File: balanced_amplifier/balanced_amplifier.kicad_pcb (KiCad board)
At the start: 2 copper layers, 100 x 100 mm, 117 parts, among them J1 Conn_01x04_Male, J2 Conn_01x04_Male, J3 Screw_Terminal_01x03, J4 Conn_01x04_Male, J5 Conn_01x04_Male, U1 LM4562, U2 LM4562, U3 NE5532, U4 LM4562, U5 LM4562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

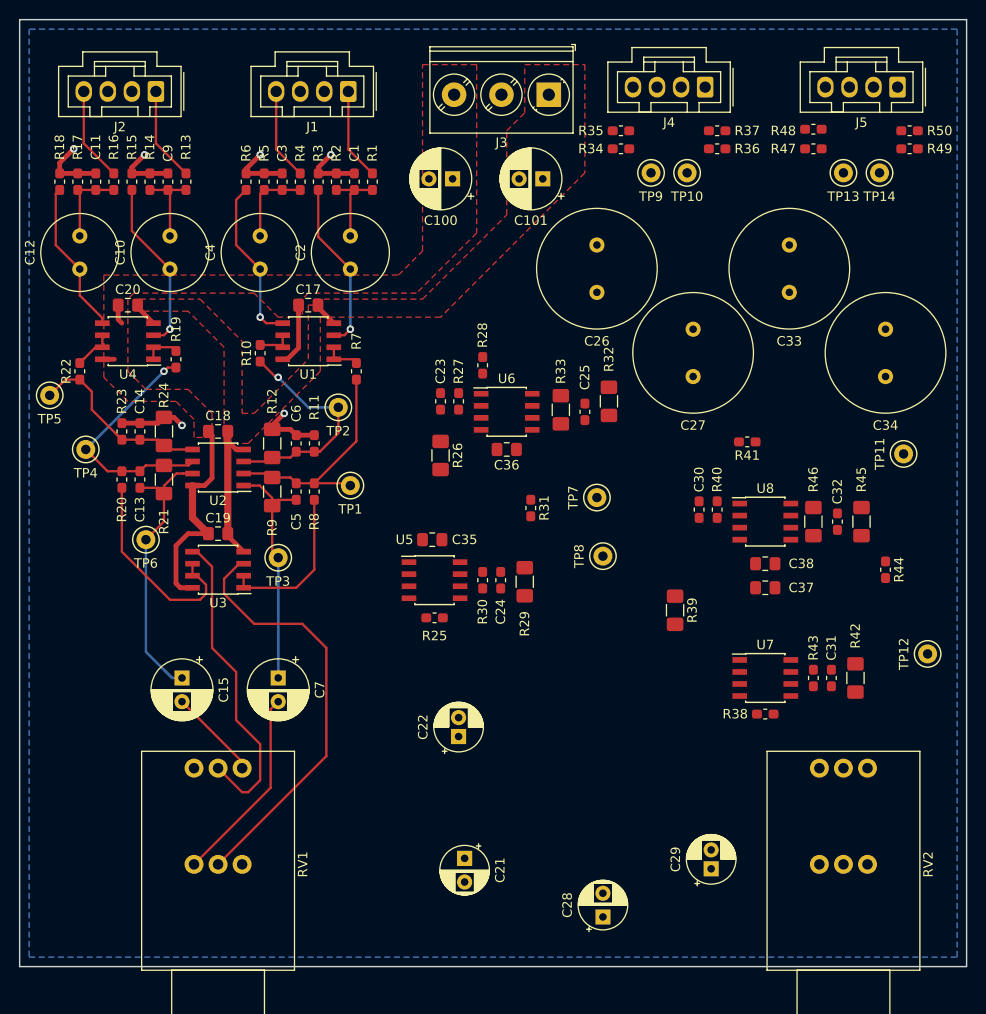
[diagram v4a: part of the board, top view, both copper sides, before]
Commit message: initial layout complete; all connections made & passes DRC
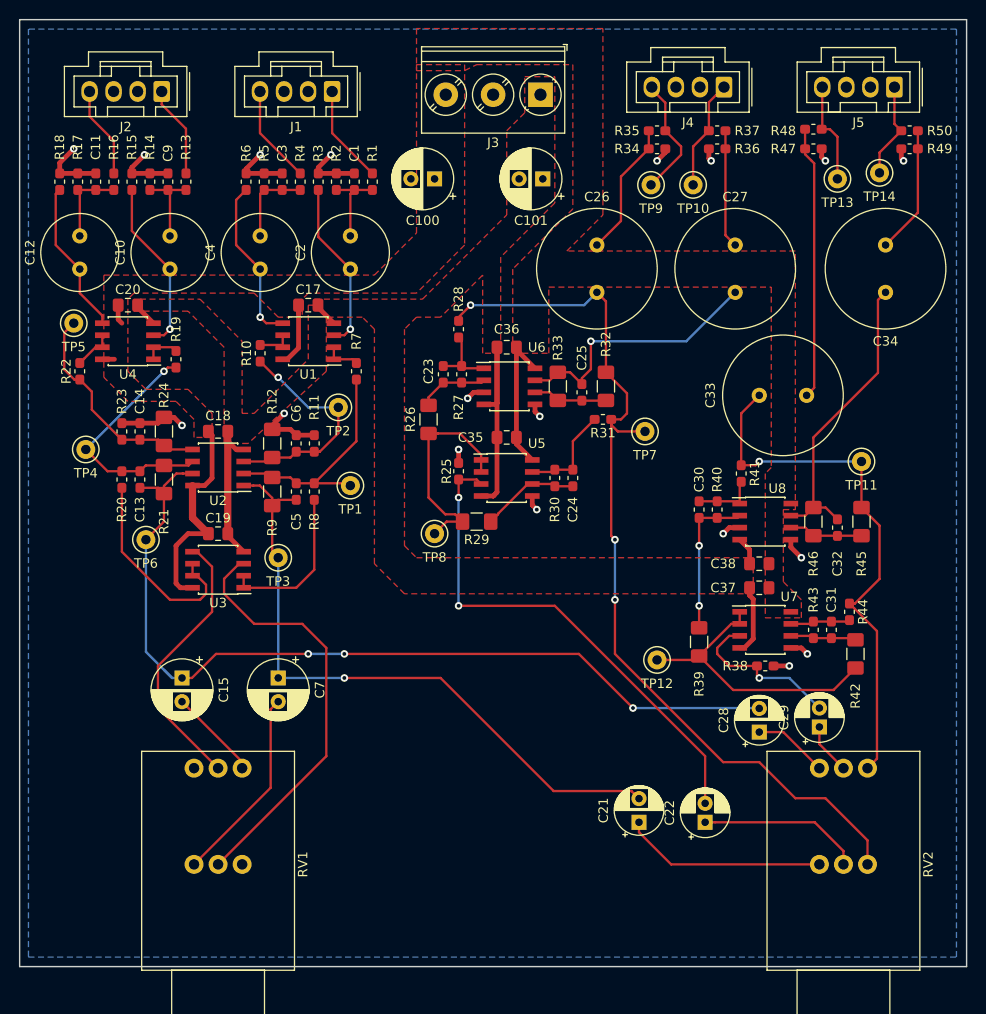
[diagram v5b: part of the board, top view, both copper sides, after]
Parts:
- moved TP12 28.6 mm to (143.5, 95.4), turned to 180 degrees
- moved C22 27.6 mm to (148.6, 112.6)
- moved C28 25.6 mm to (154.3, 103.0)
- moved C29 18.8 mm to (160.7, 102.5)
- moved C21 18.8 mm to (141.6, 112.6), turned to 90 degrees
- moved TP8 17.9 mm to (120.0, 82.1), turned to 180 degrees
- moved C33 16.0 mm to (159.3, 67.5), turned to 180 degrees
- moved R25 15.7 mm to (122.6, 75.5), turned to 90 degrees
- moved C35 13.4 mm to (127.6, 71.9)
- moved C24 13.2 mm to (134.6, 76.2)
- moved R30 13.2 mm to (132.7, 76.2)
- moved U5 13.2 mm to (127.6, 76.2)
- moved R31 12.1 mm to (137.8, 70.0), turned to 180 degrees
- moved C36 10.8 mm to (127.6, 62.4)
- moved C27 9.94 mm to (151.8, 51.6)
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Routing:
- net Net-(C26-Pad2): track 0.00 -> 98.8 mm, vias 0 -> 3
- net /volume_control/left_in: track 30.8 -> 95.2 mm, vias 0 -> 3
- net Net-(C33-Pad2): track 0.00 -> 57.5 mm, vias 0 -> 1
- net Net-(C22-Pad2): track 0.00 -> 53.5 mm, vias 0 -> 2
- net /volume_control/right_in: track 26.5 -> 69.9 mm, vias 0 -> 1
- net VEE: track 21.9 -> 57.5 mm
- net Net-(C32-Pad1): track 0.00 -> 31.7 mm
- net Net-(R39-Pad2): track 0.00 -> 30.5 mm
- net Net-(C33-Pad1): track 0.00 -> 28.8 mm
- net Net-(C25-Pad1): track 0.00 -> 28.1 mm, vias 0 -> 1
- net Net-(R26-Pad2): track 0.00 -> 23.2 mm
- net Net-(C21-Pad1): track 0.00 -> 21.5 mm
- net GNDA: track 39.9 -> 60.3 mm, vias 6 -> 18
- net Net-(C29-Pad2): track 0.00 -> 17.3 mm, vias 0 -> 1
- net Net-(C22-Pad1): track 0.00 -> 17.3 mm
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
